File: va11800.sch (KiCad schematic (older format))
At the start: 255 parts, among them J1 Conn_01x16_Female, J2 Conn_01x16_Female, j1 MX-NoLED, k1 MX-NoLED, m1 MX-NoLED, p1 MX-NoLED, q1 MX-NoLED, t1 MX-NoLED, u1 MX-NoLED, x1 MX-NoLED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

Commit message: fix footprint associations
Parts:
- D1: footprint Keebio-Parts:Diode-dual -> vuckale:Diode
- D17, D50, D52: footprint Keebio-Parts:LED_D2.00mm -> vuckale:LED_D2.00mm
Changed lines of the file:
@@
 F 0 "D17" H 14933 7107 50  0000 C CNN
 F 1 "LED" H 14933 7016 50  0000 C CNN
-F 2 "Keebio-Parts:LED_D2.00mm" H 14940 6890 50  0001 C CNN
+F 2 "vuckale:LED_D2.00mm" H 14940 6890 50  0001 C CNN
 F 3 "~" H 14940 6890 50  0001 C CNN
 	1    14940 6890
@@
 F 0 "D50" H 15293 7107 50  0000 C CNN
 F 1 "LED" H 15293 7016 50  0000 C CNN
-F 2 "Keebio-Parts:LED_D2.00mm" H 15300 6890 50  0001 C CNN
+F 2 "vuckale:LED_D2.00mm" H 15300 6890 50  0001 C CNN
 F 3 "~" H 15300 6890 50  0001 C CNN
 	1    15300 6890
@@
 F 0 "D52" H 15643 7107 50  0000 C CNN
 F 1 "LED" H 15643 7016 50  0000 C CNN
-F 2 "Keebio-Parts:LED_D2.00mm" H 15650 6890 50  0001 C CNN
+F 2 "vuckale:LED_D2.00mm" H 15650 6890 50  0001 C CNN
 F 3 "~" H 15650 6890 50  0001 C CNN
 	1    15650 6890
@@
 F 0 "D1" H 8900 8243 50  0000 C CNN
 F 1 "D_Small" H 8900 8334 50  0000 C CNN
-F 2 "Keebio-Parts:Diode-dual" V 8900 8450 50  0001 C CNN
+F 2 "vuckale:Diode" V 8900 8450 50  0001 C CNN
 F 3 "~" V 8900 8450 50  0001 C CNN
 	1    8900 8450

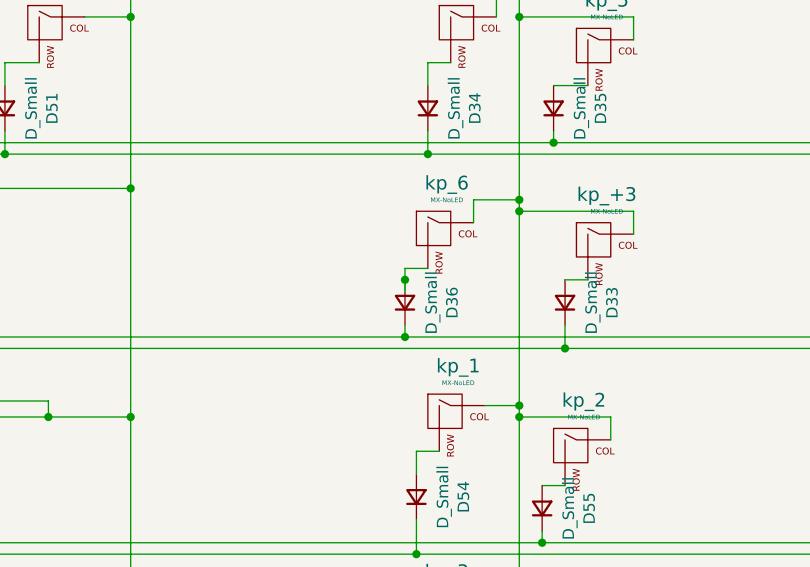
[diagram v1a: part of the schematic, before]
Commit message: add github repository silkscreen
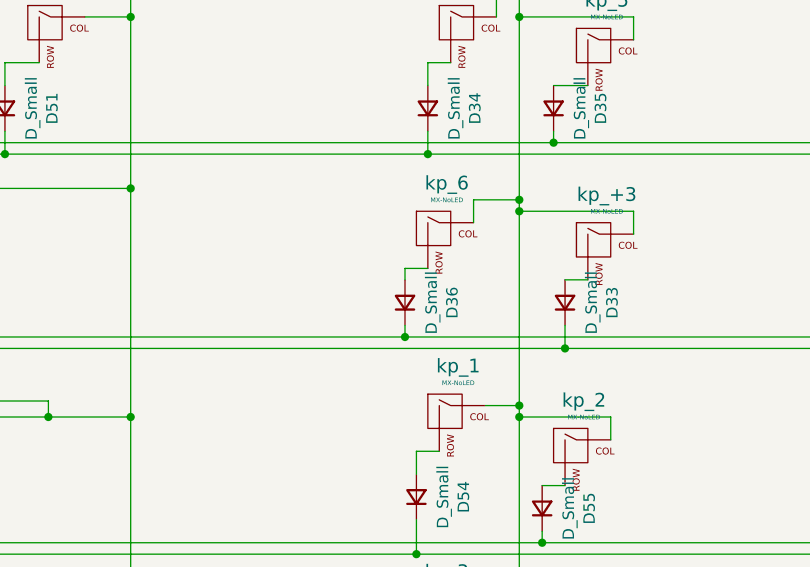
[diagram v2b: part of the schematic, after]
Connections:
- wire segments 836 -> 835
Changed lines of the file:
@@
 Wire Wire Line
 	17300 11150 17300 11200
-Connection ~ 17300 11200
-Wire Wire Line
-	17300 11200 17300 11250
 Wire Wire Line
 	17800 10900 17800 11750

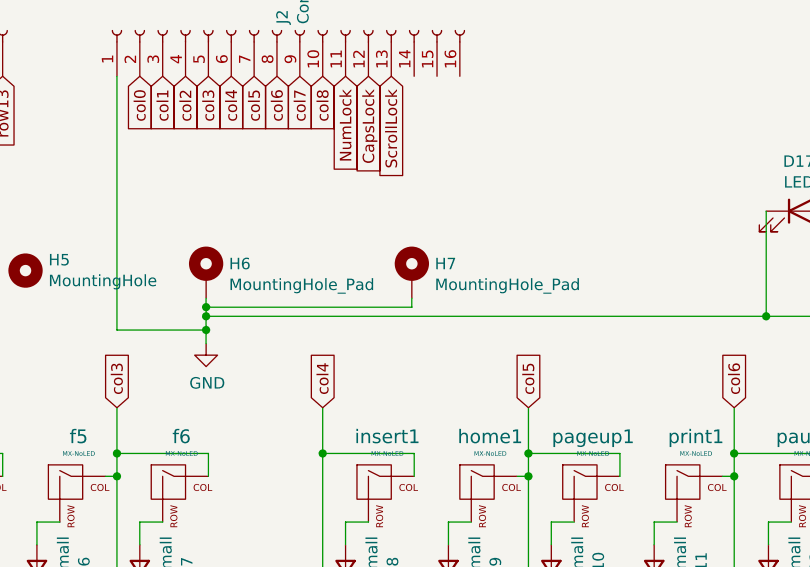
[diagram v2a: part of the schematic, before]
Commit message: modify GND pad
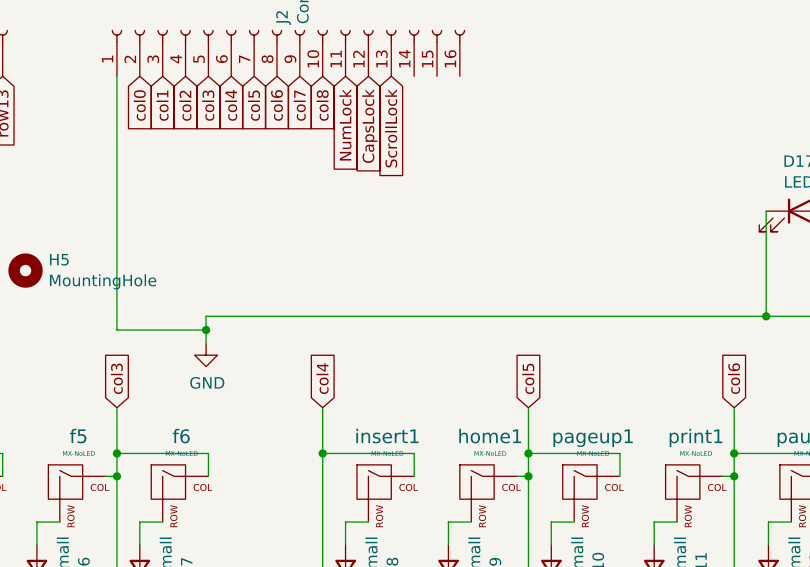
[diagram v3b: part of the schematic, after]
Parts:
- removed H6, H7: MountingHole_Pad, Keebio-Parts:SolidCopper, symbol Mechanical:MountingHole_Pad
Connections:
- wire segments 835 -> 831
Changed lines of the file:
@@
 	8900 11100 8900 11200
-$Comp
-L Mechanical:MountingHole_Pad H7
-U 1 1 620D9A4A
-P 13240 7170
-F 0 "H7" H 13340 7219 50  0000 L CNN
-F 1 "MountingHole_Pad" H 13340 7128 50  0000 L CNN
-F 2 "Keebio-Parts:SolidCopper" H 13240 7170 50  0001 C CNN
-F 3 "~" H 13240 7170 50  0001 C CNN
-	1    13240 7170
-	1    0    0    -1
-$EndComp
 $Comp
 L power:GND #PWR0102
@@
 	1    0    0    -1
 $EndComp
-$Comp
-L Mechanical:MountingHole_Pad H6
-U 1 1 62315ACB
-P 12340 7170
-F 0 "H6" H 12440 7219 50  0000 L CNN
-F 1 "MountingHole_Pad" H 12440 7128 50  0000 L CNN
-F 2 "Keebio-Parts:SolidCopper" H 12340 7170 50  0001 C CNN
-F 3 "~" H 12340 7170 50  0001 C CNN
-	1    12340 7170
-	1    0    0    -1
-$EndComp
-Wire Wire Line
-	12340 7270 12340 7310
-Wire Wire Line
-	13240 7270 13240 7310
-Wire Wire Line
-	13240 7310 12340 7310
-Connection ~ 12340 7310
-Wire Wire Line
-	12340 7310 12340 7350
 $Comp
 L Device:LED D17
@@
 Wire Wire Line
 	15510 7350 15500 6890
-Connection ~ 12340 7350
 Wire Wire Line
 	15150 6890 15150 7350
